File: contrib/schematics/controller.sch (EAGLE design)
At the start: 31 parts, among them IC2 MAX 603, IC3 MEGA16-P, Q1 16 MHz, T1 BS-107, T2 BS-107

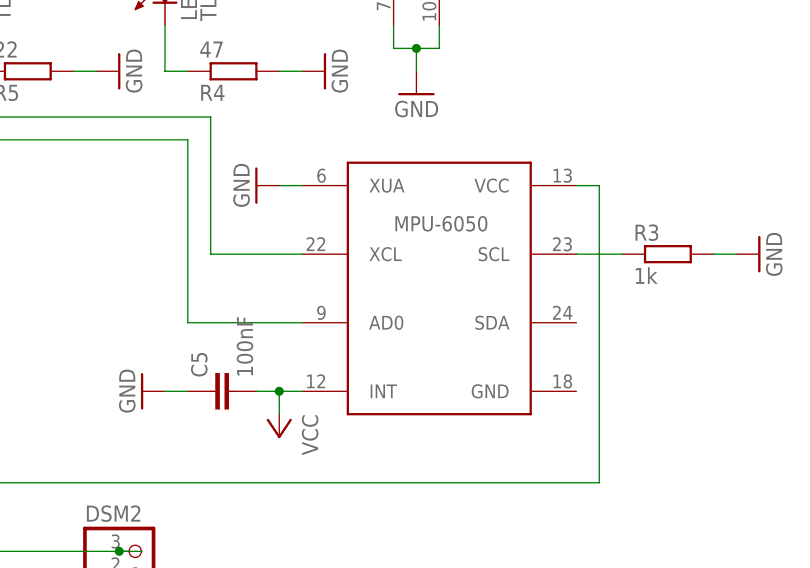
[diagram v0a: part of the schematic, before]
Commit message: Implementing MPU-6050
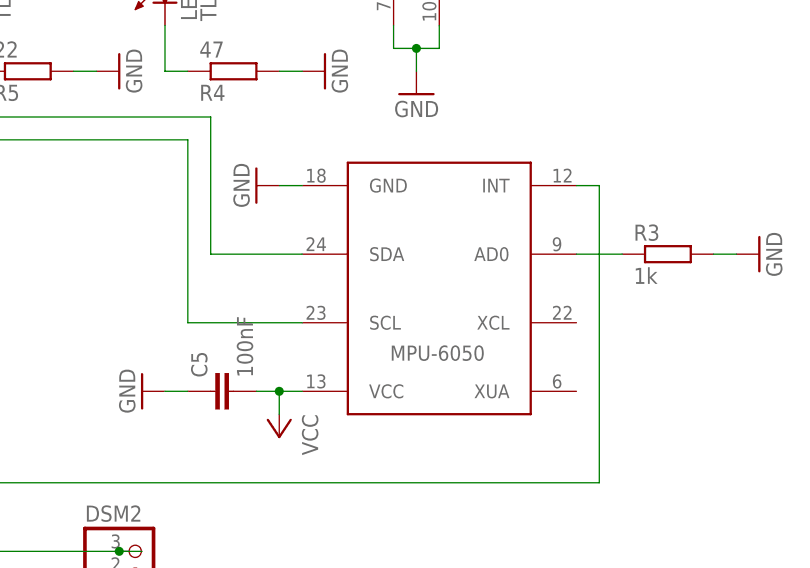
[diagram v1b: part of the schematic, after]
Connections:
- net GND: now also U$1.GND; no longer U$1.XUA
- net N$10: now also U$1.INT; no longer U$1.VCC
- net N$17: now also U$1.SCL; no longer U$1.AD0
- net N$18: now also U$1.SDA; no longer U$1.XCL
- net N$5: now also U$1.AD0; no longer U$1.SCL
- net VCC: now also U$1.VCC; no longer U$1.INT
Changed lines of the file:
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@@
 <instance part="P+3" gate="VCC" x="68.58" y="5.08" rot="R90"/>
 <instance part="P+9" gate="VCC" x="68.58" y="-7.62" rot="R90"/>
-<instance part="U$1" gate="G$1" x="139.7" y="-96.52"/>
+<instance part="U$1" gate="G$1" x="139.7" y="-99.06" rot="R180"/>
 </instances>
 <busses>
@@
 <nets>
 <net name="GND" class="0">
-<segment>
-<pinref part="GND2" gate="1" pin="GND"/>
-<wire x1="121.92" y1="-86.36" x2="124.46" y2="-86.36" width="0.1524" layer="91"/>
-<pinref part="U$1" gate="G$1" pin="XUA"/>
-</segment>
 <segment>
 <pinref part="R3" gate="G$1" pin="2"/>
@@
 <junction x="81.28" y="22.86"/>
 </segment>
+<segment>
+<pinref part="GND2" gate="1" pin="GND"/>
+<pinref part="U$1" gate="G$1" pin="GND"/>
+<wire x1="121.92" y1="-86.36" x2="124.46" y2="-86.36" width="0.1524" layer="91"/>
+</segment>
 </net>
 <net name="VCC" class="0">
@@
 </segment>
 <segment>
-<wire x1="124.46" y1="-109.22" x2="121.92" y2="-109.22" width="0.1524" layer="91"/>
 <pinref part="P+8" gate="VCC" pin="VCC"/>
 <pinref part="C5" gate="G$1" pin="2"/>
 <wire x1="121.92" y1="-109.22" x2="121.92" y2="-111.76" width="0.1524" layer="91"/>
 <wire x1="119.38" y1="-109.22" x2="121.92" y2="-109.22" width="0.1524" layer="91"/>
+<pinref part="U$1" gate="G$1" pin="VCC"/>
+<wire x1="121.92" y1="-109.22" x2="124.46" y2="-109.22" width="0.1524" layer="91"/>
 <junction x="121.92" y="-109.22"/>
-<pinref part="U$1" gate="G$1" pin="INT"/>
 </segment>
 <segment>
@@
 </segment>
 </net>
-<net name="N$5" class="0">
-<segment>
-<pinref part="R3" gate="G$1" pin="1"/>
-<wire x1="160.02" y1="-93.98" x2="154.94" y2="-93.98" width="0.1524" layer="91"/>
-<pinref part="U$1" gate="G$1" pin="SCL"/>
-</segment>
-</net>
 <net name="N$2" class="0">
 <segment>
@@
 <wire x1="78.74" y1="-81.28" x2="111.76" y2="-81.28" width="0.1524" layer="91"/>
 <wire x1="111.76" y1="-81.28" x2="111.76" y2="-101.6" width="0.1524" layer="91"/>
-<wire x1="111.76" y1="-101.6" x2="124.46" y2="-101.6" width="0.1524" layer="91"/>
 <pinref part="T1" gate="G$1" pin="S"/>
 <wire x1="78.74" y1="2.54" x2="78.74" y2="-81.28" width="0.1524" layer="91"/>
 <junction x="78.74" y="-81.28"/>
-<pinref part="U$1" gate="G$1" pin="AD0"/>
+<pinref part="U$1" gate="G$1" pin="SCL"/>
+<wire x1="124.46" y1="-101.6" x2="111.76" y2="-101.6" width="0.1524" layer="91"/>
 </segment>
 </net>
 <net name="N$10" class="0">
 <segment>
-<wire x1="157.48" y1="-86.36" x2="154.94" y2="-86.36" width="0.1524" layer="91"/>
 <pinref part="IC3" gate="G$1" pin="(INT1)PD3"/>
 <wire x1="76.2" y1="-96.52" x2="86.36" y2="-96.52" width="0.1524" layer="91"/>
@@
 <wire x1="86.36" y1="-119.38" x2="157.48" y2="-119.38" width="0.1524" layer="91"/>
 <wire x1="157.48" y1="-119.38" x2="157.48" y2="-86.36" width="0.1524" layer="91"/>
-<pinref part="U$1" gate="G$1" pin="VCC"/>
+<pinref part="U$1" gate="G$1" pin="INT"/>
+<wire x1="157.48" y1="-86.36" x2="154.94" y2="-86.36" width="0.1524" layer="91"/>
 </segment>
 </net>
 <net name="N$18" class="0">
 <segment>
-<wire x1="124.46" y1="-93.98" x2="114.3" y2="-93.98" width="0.1524" layer="91"/>
 <wire x1="114.3" y1="-93.98" x2="114.3" y2="-78.74" width="0.1524" layer="91"/>
 <pinref part="IC3" gate="G$1" pin="(SDA)PC1"/>
@@
 <wire x1="81.28" y1="-12.7" x2="81.28" y2="-78.74" width="0.1524" layer="91"/>
 <junction x="81.28" y="-78.74"/>
-<pinref part="U$1" gate="G$1" pin="XCL"/>
+<pinref part="U$1" gate="G$1" pin="SDA"/>
+<wire x1="114.3" y1="-93.98" x2="124.46" y2="-93.98" width="0.1524" layer="91"/>
 </segment>
 </net>
@@
 </segment>
 </net>
+<net name="N$5" class="0">
+<segment>
+<pinref part="U$1" gate="G$1" pin="AD0"/>
+<pinref part="R3" gate="G$1" pin="1"/>
+<wire x1="154.94" y1="-93.98" x2="160.02" y2="-93.98" width="0.1524" layer="91"/>
+</segment>
+</net>

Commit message: Updated controller board
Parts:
- added JP2: AVR-ISP-6VERT, avr-7:AVR-ISP-6VERT
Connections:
- net GND: now also JP2.6
- net N$12: now also JP2.4
- net N$14: now also JP2.1
- net N$15: now also JP2.3
- net N$24: now also C11.1
- net N$9: now also JP2.5
- net VCC: now also JP2.2
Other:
- moved on the sheet: ANT1, C10, C11, C4, C8, D1, IC2, JP1, JP5, R2, S1, T1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

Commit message: Updated telemetrics board
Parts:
- IC2: value MAX 603 -> MAX 604
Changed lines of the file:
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@@
 <part name="C7" library="capacitor-wima" deviceset="C" device="2.5/2" value="22pF"/>
 <part name="GND1" library="supply1" deviceset="GND" device=""/>
-<part name="IC2" library="ic-package" deviceset="DIL8" device="S" value="MAX 603"/>
+<part name="IC2" library="ic-package" deviceset="DIL8" device="S" value="MAX 604"/>
 <part name="C8" library="capacitor-wima" deviceset="C" device="2.5/6" value="220µF"/>
 <part name="C10" library="capacitor-wima" deviceset="C" device="2.5/5" value="10µF"/>
